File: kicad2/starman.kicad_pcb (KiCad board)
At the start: 2 copper layers, 160 x 150 mm, 183 parts, among them J1 Conn_01x10, J2 Conn_01x10, J3 Conn_01x10, U1 ESP32-S2-MINI-1, U2 PCA9959, U3 PCA9959, U4 PCA9959, U5 PCA9959, U6 LF33_TO220, U7 MIC29310-5.0WU, U8 PCA9959, U9 PCA9959, Y1 20Mhz, Y2 20Mhz, Y3 20Mhz, Y4 20Mhz, Y5 20Mhz, Y6 20Mhz

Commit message: Transition to kicad v6
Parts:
- J1: renamed from J2; value Conn_01x10 -> Conn_01x12; footprint Connector_PinHeader_2.00mm:PinHeader_1x10_P2.00mm_Vertical_SMD_Pin1Left -> Connector_PinSocket_2.54mm:PinSocket_1x12_P2.54mm_Vertical_SMD_Pin1Right
- J2: renamed from J1; footprint Connector_PinHeader_2.00mm:PinHeader_1x06_P2.00mm_Vertical_SMD_Pin1Left -> Connector_PinSocket_2.54mm:PinSocket_1x06_P2.54mm_Vertical_SMD_Pin1Left
- J3: value Conn_01x10 -> Conn_01x12; footprint Connector_PinHeader_2.00mm:PinHeader_1x10_P2.00mm_Vertical_SMD_Pin1Right -> Connector_PinSocket_2.54mm:PinSocket_1x12_P2.54mm_Vertical_SMD_Pin1Left
- U8: renamed from U6; value LF33_TO220 -> MIC29310-5.0WU; footprint Package_TO_SOT_SMD:SOT-223 -> Package_TO_SOT_SMD:TO-263-3_TabPin2
- U9: renamed from U7; value MIC29310-5.0WU -> LF33_TO220; footprint Package_TO_SOT_SMD:TO-263-3_TabPin2 -> Package_TO_SOT_SMD:SOT-223-3_TabPin2
- moved R3 48.0 mm to (127.5, 88.0), turned to -90 degrees
- moved R4 44.9 mm to (122.5, 88.0), turned to -90 degrees
- moved U8 29.7 mm to (125.0, 98.5), turned to 90 degrees
- moved U9 29.2 mm to (96.5, 105.8), turned to 0 degrees
- moved C12 25.5 mm to (60.0, 135.0)
- moved C9 20.9 mm to (80.0, 95.1), turned to 0 degrees
- moved C8 19.3 mm to (110.0, 84.0)
- moved C10 8.09 mm to (158.0, 95.0), turned to -90 degrees
- moved J1 5.00 mm to (120.0, 130.0)
- moved J2 5.00 mm to (110.0, 95.0)
- moved J3 5.00 mm to (100.0, 130.0)
- moved C11 4.23 mm to (110.0, 135.0), turned to 0 degrees
- moved R9 3.84 mm to (65.0, 140.0), turned to 180 degrees
- moved C13 2.25 mm to (160.0, 135.0)
- moved Y5 0.51 mm to (140.6, 91.6)
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- renumbered U8 to U6, U9 to U7
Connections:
- C4 pad 2: Net-(C4-Pad2) -> +5V
- C6 pad 2: Net-(C4-Pad2) -> Net-(C6-Pad2)
- J1 pad 1: Net-(C4-Pad2) -> Net-(C6-Pad2)
- J1 pad 10: (no net) -> /GPIO6
- J1 pad 2: Net-(C4-Pad2) -> unconnected-(J1-Pad2)
- J1 pad 3: GND -> unconnected-(J1-Pad3)
- J1 pad 4: GND -> unconnected-(J1-Pad4)
- J1 pad 5: (no net) -> /GPIO1
- J1 pad 6: (no net) -> /GPIO2
- J1 pad 7: (no net) -> /GPIO3
- J1 pad 8: (no net) -> /GPIO4
- J1 pad 9: (no net) -> /GPIO5
- J2 pad 1: /TXD -> /RXD
- J2 pad 2: /RXD -> /TXD
- J2 pad 5: /USBDM -> /USBDP
- J2 pad 6: /USBDP -> /USBDM
- J3 pad 1: (no net) -> +3V3
- J3 pad 10: (no net) -> /GPIO16
- J3 pad 2: (no net) -> GND
- J3 pad 3: (no net) -> /GPIO9
- J3 pad 4: (no net) -> /GPIO10
- J3 pad 5: (no net) -> /GPIO11
- J3 pad 6: (no net) -> /GPIO12
- J3 pad 7: (no net) -> /GPIO13
- J3 pad 8: (no net) -> /GPIO14
- J3 pad 9: (no net) -> /GPIO15
- R3 pad 1: /RESET -> +3V3
- R3 pad 2: +3V3 -> /RESET
- R4 pad 1: /OE -> +3V3
- R4 pad 2: +3V3 -> /OE
- U1 pad 10: /MISO -> /GPIO6
- U1 pad 11: /RESET -> /GPIO7
- U1 pad 12: (no net) -> /GPIO8
- U1 pad 13: (no net) -> /GPIO9
- U1 pad 14: (no net) -> /GPIO10
- U1 pad 15: (no net) -> /GPIO11
- U1 pad 16: (no net) -> /GPIO12
- U1 pad 17: (no net) -> /GPIO13
- U1 pad 18: (no net) -> /GPIO14
- U1 pad 19: (no net) -> /GPIO15
- U1 pad 20: (no net) -> /GPIO16
- U1 pad 21: (no net) -> unconnected-(U1-Pad21)
- U1 pad 22: (no net) -> unconnected-(U1-Pad22)
- U1 pad 25: (no net) -> unconnected-(U1-Pad25)
- U1 pad 26: (no net) -> unconnected-(U1-Pad26)
- U1 pad 27: (no net) -> unconnected-(U1-Pad27)
- U1 pad 28: (no net) -> /RESET
- U1 pad 29: (no net) -> /MISO
- U1 pad 31: (no net) -> /MOSI
- U1 pad 32: (no net) -> /SCLK
- U1 pad 33: (no net) -> /CS
- U1 pad 34: (no net) -> /OE
- U1 pad 35: (no net) -> unconnected-(U1-Pad35)
- U1 pad 36: (no net) -> unconnected-(U1-Pad36)
- U1 pad 37: (no net) -> unconnected-(U1-Pad37)
- U1 pad 38: (no net) -> unconnected-(U1-Pad38)
- U1 pad 41: (no net) -> unconnected-(U1-Pad41)
- U1 pad 44: (no net) -> unconnected-(U1-Pad44)
- U1 pad 5: (no net) -> /GPIO1
- U1 pad 6: /OE -> /GPIO2
- U1 pad 7: /CS -> /GPIO3
- U1 pad 8: /SCLK -> /GPIO4
- U1 pad 9: /MOSI -> /GPIO5
- U2 pad 11: (no net) -> unconnected-(U2-Pad11)
- U2 pad 12: (no net) -> unconnected-(U2-Pad12)
- U2 pad 21: (no net) -> unconnected-(U2-Pad21)
- U3 pad 11: (no net) -> unconnected-(U3-Pad11)
- U3 pad 12: (no net) -> unconnected-(U3-Pad12)
- U3 pad 21: (no net) -> unconnected-(U3-Pad21)
- U4 pad 11: (no net) -> unconnected-(U4-Pad11)
- U4 pad 12: (no net) -> unconnected-(U4-Pad12)
- U4 pad 21: (no net) -> unconnected-(U4-Pad21)
- U5 pad 11: (no net) -> unconnected-(U5-Pad11)
- U5 pad 12: (no net) -> unconnected-(U5-Pad12)
- U5 pad 21: (no net) -> unconnected-(U5-Pad21)
- U6 pad 11: (no net) -> unconnected-(U6-Pad11)
- U6 pad 12: (no net) -> unconnected-(U6-Pad12)
- U6 pad 21: (no net) -> unconnected-(U6-Pad21)
- U7 pad 11: (no net) -> unconnected-(U7-Pad11)
- U7 pad 12: (no net) -> unconnected-(U7-Pad12)
- U7 pad 21: (no net) -> unconnected-(U7-Pad21)
- U8 pad 1: Net-(C4-Pad2) -> Net-(C6-Pad2)
- U8 pad 3: +3V3 -> +5V
- U9 pad 1: Net-(C4-Pad2) -> +5V
- U9 pad 3: +5V -> +3V3
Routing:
- net GND: track 572.0 -> 221.6 mm, vias 29 -> 28
- net +5V: track 413.7 -> 186.9 mm, vias 66 -> 39
- net Net-(C4-Pad2): track 64.2 -> 0.00 mm, vias 4 -> 0
- net /CS: track 265.7 -> 306.3 mm, vias 9 -> 8
- net +3V3: track 287.4 -> 324.4 mm, vias 13 -> 12
- net /OE: track 270.1 -> 297.5 mm, vias 12 -> 11
- net /MISO: track 108.7 -> 84.6 mm, vias 6 -> 2
- net Net-(C6-Pad2): track 0.00 -> 12.9 mm
- net Net-(D52-Pad1): track 44.7 -> 32.0 mm, vias 0 -> 2
- net Net-(U4-Pad4): track 63.8 -> 52.9 mm
- net /SCLK: track 273.7 -> 283.8 mm, vias 6 -> 11
- net Net-(D83-Pad1): track 15.0 -> 23.3 mm
- net /MOSI: track 42.8 -> 35.1 mm
- net Net-(D86-Pad1): track 15.0 -> 22.7 mm
- net /RESET: track 273.0 -> 265.6 mm, vias 11 -> 8
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- added copper zone on In1.Cu, net GND
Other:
- copper layers 2 -> 4
- net class Default removed

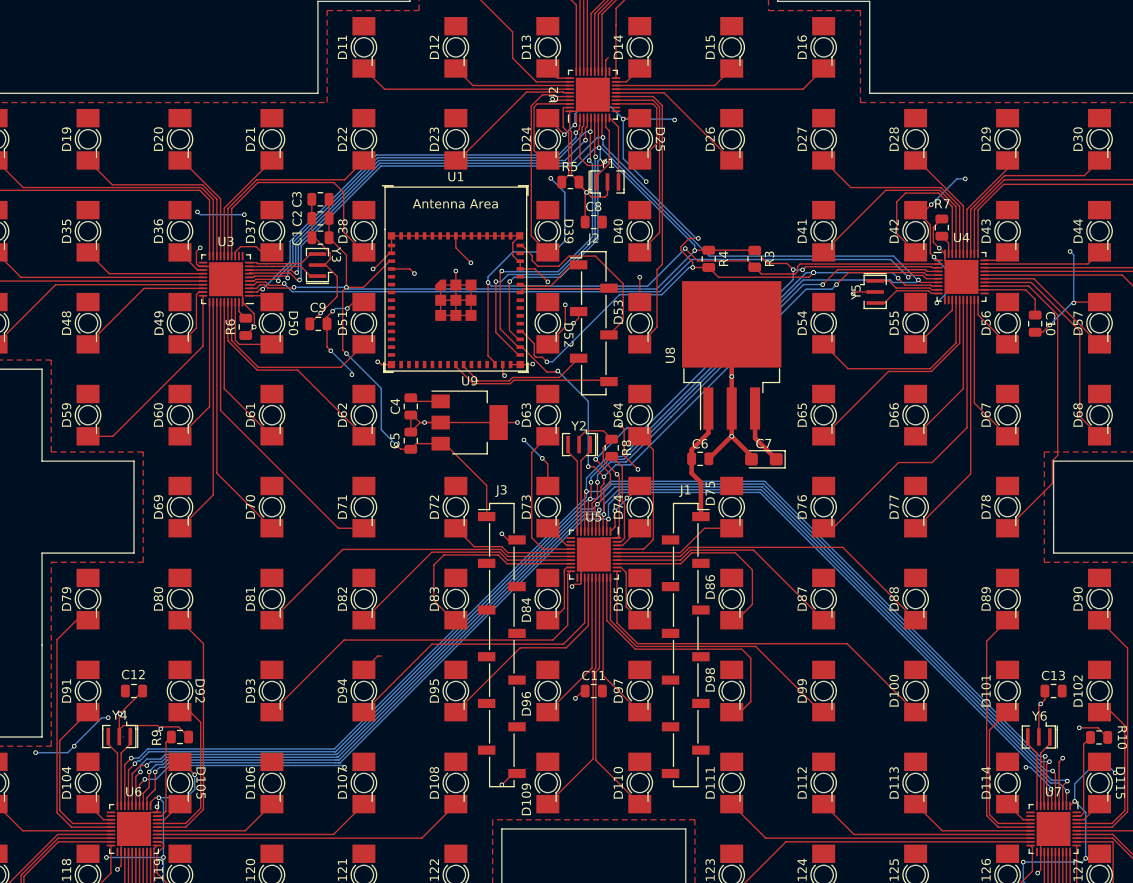
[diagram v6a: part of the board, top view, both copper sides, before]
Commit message: Complete routing of all GPIO pins
Also fixed paths to 3d components
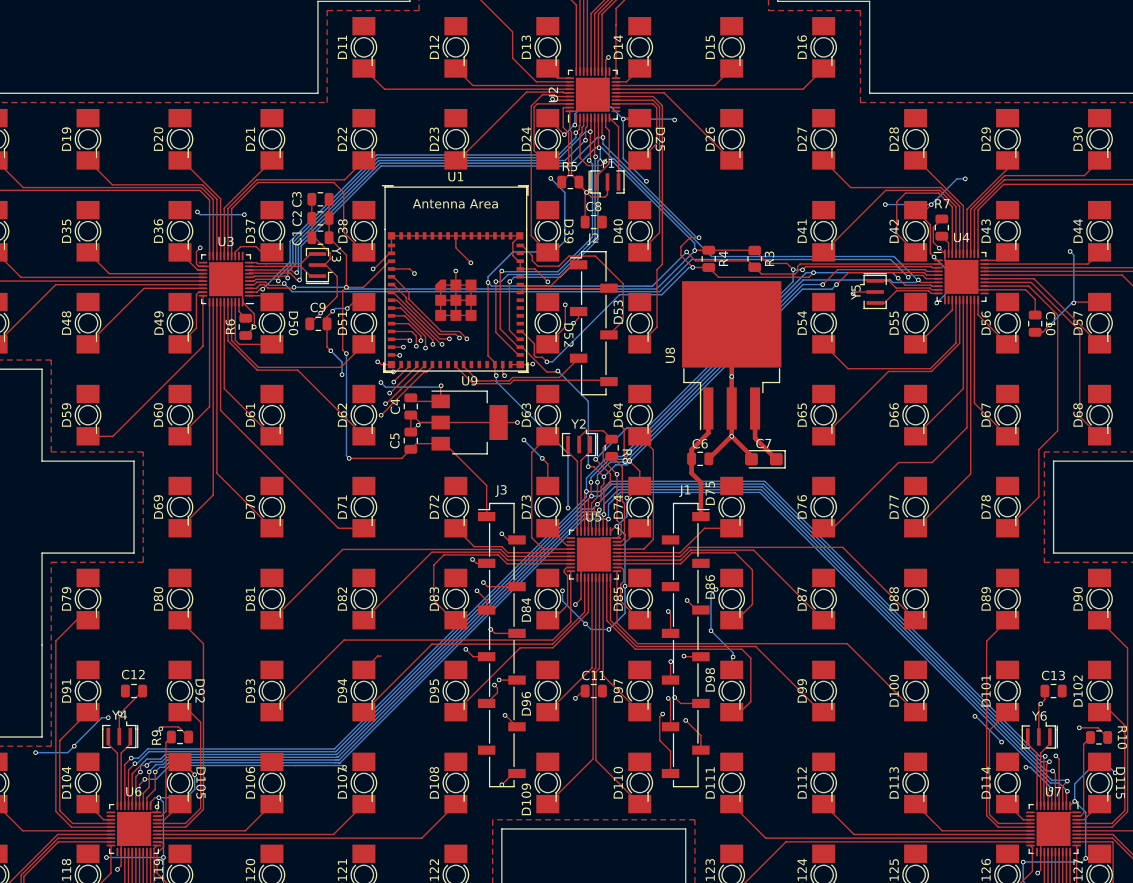
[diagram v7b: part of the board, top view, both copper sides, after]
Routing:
- net /GPIO8: track 0.00 -> 62.2 mm, vias 0 -> 2
- net /GPIO7: track 0.00 -> 61.5 mm, vias 0 -> 2
- net /GPIO5: track 0.00 -> 58.8 mm, vias 0 -> 2
- net /GPIO6: track 0.00 -> 58.1 mm, vias 0 -> 2
- net /GPIO3: track 0.00 -> 55.7 mm, vias 0 -> 2
- net /GPIO4: track 0.00 -> 54.8 mm, vias 0 -> 2
- net /GPIO1: track 0.00 -> 52.4 mm, vias 0 -> 2
- net /GPIO2: track 0.00 -> 51.7 mm, vias 0 -> 2
- net /GPIO16: track 0.00 -> 48.0 mm, vias 0 -> 2
- net +5V: track 186.9 -> 232.8 mm, vias 39 -> 48
- net /GPIO15: track 0.00 -> 44.4 mm, vias 0 -> 2
- net /GPIO14: track 0.00 -> 43.1 mm, vias 0 -> 2
- net /GPIO13: track 0.00 -> 37.7 mm, vias 0 -> 2
- net /GPIO12: track 0.00 -> 36.7 mm, vias 0 -> 2
- net /GPIO10: track 0.00 -> 34.3 mm, vias 0 -> 2
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
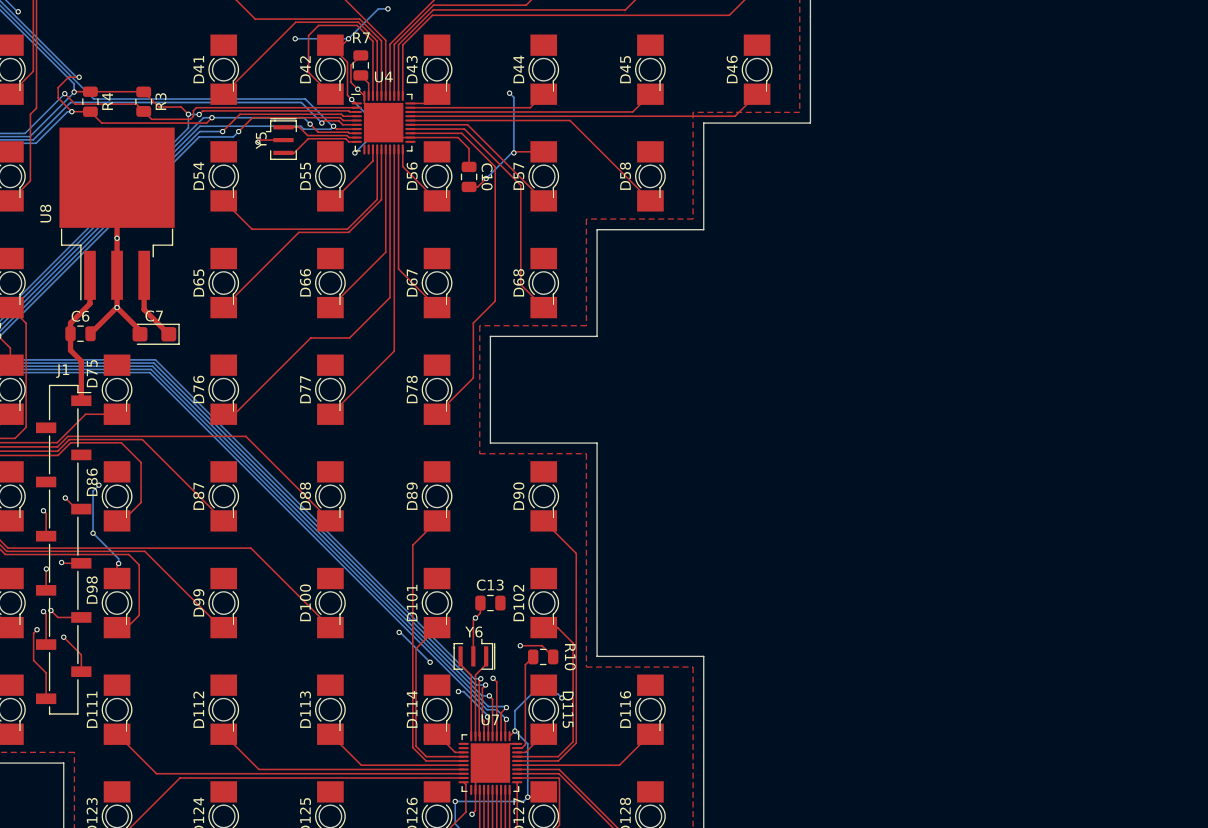
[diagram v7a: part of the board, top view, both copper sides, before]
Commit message: Added daughter board for power and buttons
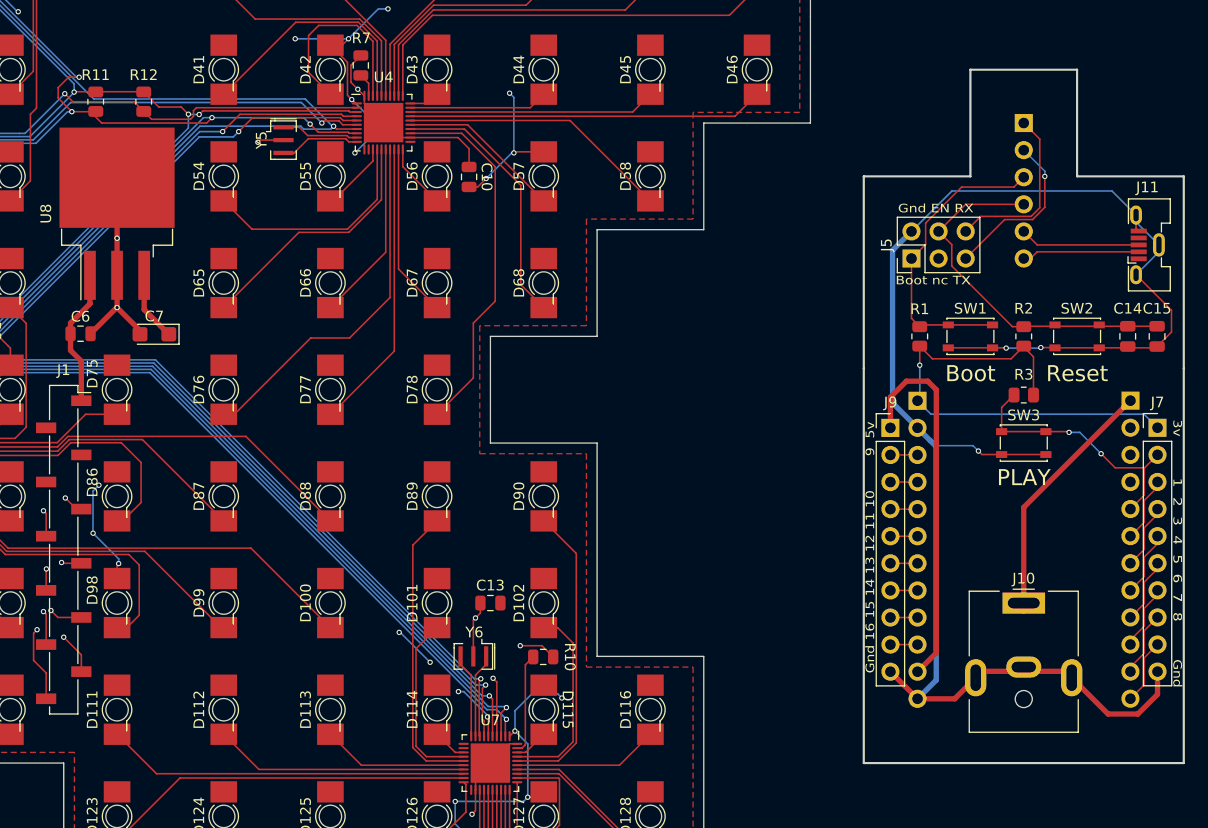
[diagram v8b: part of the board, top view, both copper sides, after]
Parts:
- removed R4: 10k, Resistor_SMD:R_0805_2012Metric
- added C14: 0.1uF, Capacitor_SMD:C_0805_2012Metric, F.Cu at (219.8, 110.0)
- added C15: 1uF, Capacitor_SMD:C_0805_2012Metric, F.Cu at (222.5, 110.0)
- added J10: Barrel_Jack_MountingPin, Connector_BarrelJack:BarrelJack_CUI_PJ-063AH_Horizontal, F.Cu at (210.0, 135.0)
- added J11: USB_B_Micro, Connector_USB:USB_Micro-B_Molex-105133-0031, F.Cu at (221.6, 101.4)
- added J4: Conn_01x10, Connector_PinHeader_2.54mm:PinHeader_1x06_P2.54mm_Vertical, B.Cu at (210.0, 90.0)
- added J5: Conn_02x03_Counter_Clockwise, Connector_PinHeader_2.54mm:PinHeader_2x03_P2.54mm_Vertical, F.Cu at (199.5, 102.7)
- added J6: Conn_01x12, Connector_PinHeader_2.54mm:PinHeader_1x12_P2.54mm_Vertical, B.Cu at (220.0, 116.0)
- added J7: Conn_01x10, Connector_PinHeader_2.54mm:PinHeader_1x10_P2.54mm_Vertical, F.Cu at (222.5, 118.6)
- added J8: Conn_01x12, Connector_PinHeader_2.54mm:PinHeader_1x12_P2.54mm_Vertical, B.Cu at (200.0, 116.0)
- added J9: Conn_01x08, Connector_PinHeader_2.54mm:PinHeader_1x10_P2.54mm_Vertical, F.Cu at (197.5, 118.6)
- added R1: 10k, Resistor_SMD:R_0805_2012Metric, F.Cu at (200.2, 110.0)
- added R11: 10k, Resistor_SMD:R_0805_2012Metric, F.Cu at (123.0, 88.0)
- added R12: 10k, Resistor_SMD:R_0805_2012Metric, F.Cu at (127.5, 88.0)
- added R2: 10k, Resistor_SMD:R_0805_2012Metric, F.Cu at (210.0, 110.0)
- added SW1: SW_SPST, Button_Switch_SMD:SW_SPST_PTS810, F.Cu at (205.0, 110.0)
- added SW2: SW_SPST, Button_Switch_SMD:SW_SPST_PTS810, F.Cu at (215.0, 110.0)
- added SW3: SW_SPST, Button_Switch_SMD:SW_SPST_PTS810, F.Cu at (210.0, 120.0)
- moved R3 87.0 mm to (210.0, 115.5), turned to 0 degrees
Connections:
- net /BOOT renamed /GPIO0
- net /ESP_RESET renamed /EN
- R3 pad 1: +3V3 -> /ext_GPIO1
- R3 pad 2: /RESET -> +3.3VA
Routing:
- net GNDA: track 0.00 -> 151.3 mm, vias 0 -> 3
- net +3.3VA: track 0.00 -> 44.5 mm, vias 0 -> 1
- net +5VA: track 0.00 -> 35.3 mm
- net /ext_EN: track 0.00 -> 34.4 mm
- net /ext_GPIO0: track 0.00 -> 28.5 mm
- net /ext_GPIO1: track 0.00 -> 24.8 mm, vias 0 -> 2
- net VCC: track 0.00 -> 23.9 mm
- net /ext_RXD: track 0.00 -> 16.4 mm
- net /ext_TXD: track 0.00 -> 15.6 mm, vias 0 -> 1
- net /ext_USBDP: track 0.00 -> 11.3 mm
- net /ext_USBDM: track 0.00 -> 11.0 mm
- net /ext_GPIO8: track 0.00 -> 6.13 mm
- net /ext_GPIO7: track 0.00 -> 6.13 mm
- net /ext_GPIO5: track 0.00 -> 6.13 mm
- net /ext_GPIO4: track 0.00 -> 6.13 mm
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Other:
- board size 160 x 150 mm -> 195 x 150 mm
- board text added: "1 2 3 4 5 6 7 8"
- board text added: "3v"
- board text added: "9 5v"
- board text added: "Boot"
- board text added: "Boot nc TX"
- board text added: "Gnd"
- board text added: "Gnd 16 15 14 13 12 11 10"
- board text added: "Gnd EN RX"
- board text added: "PLAY"
- board text added: "Reset"
